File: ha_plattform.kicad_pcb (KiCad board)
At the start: 2 copper layers, 60 x 55 mm, 12 parts, among them J3 Raspberry_Pi_2_3

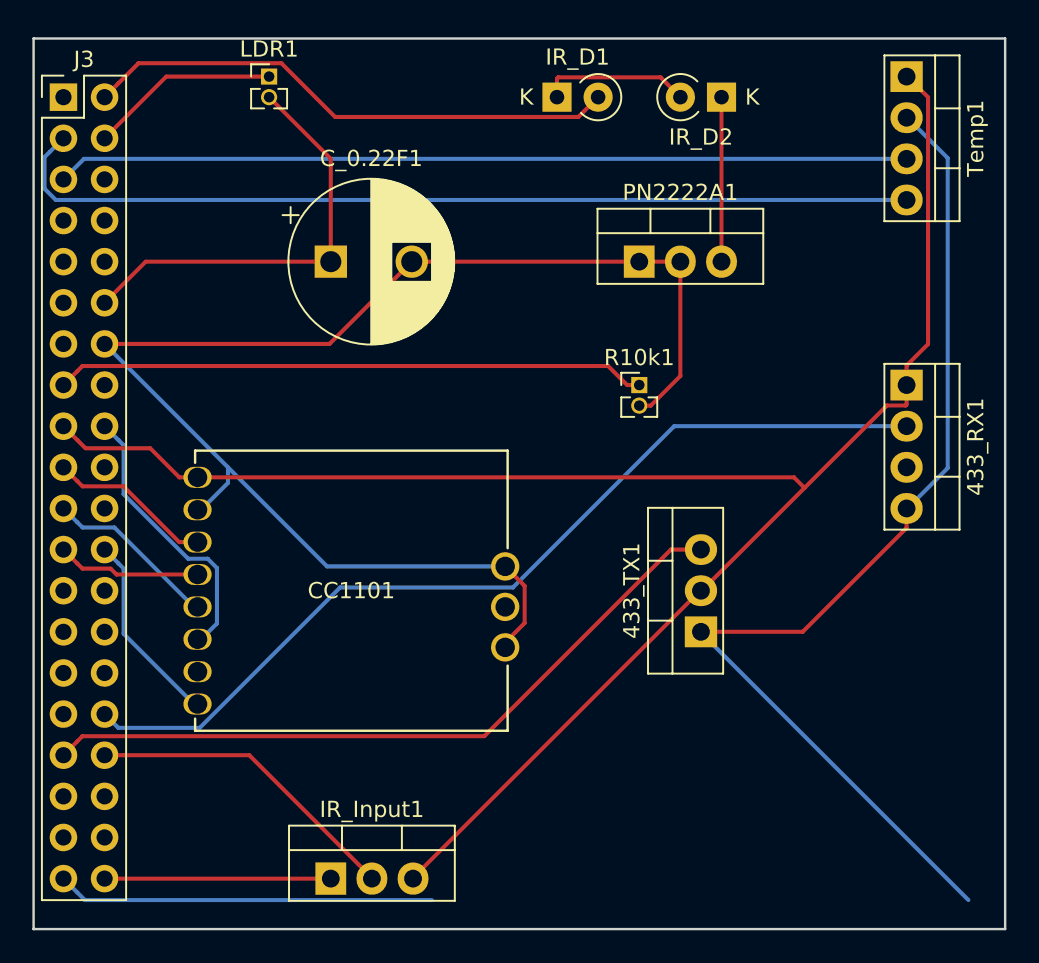
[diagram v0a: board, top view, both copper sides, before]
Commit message: Changed track width, improved routing
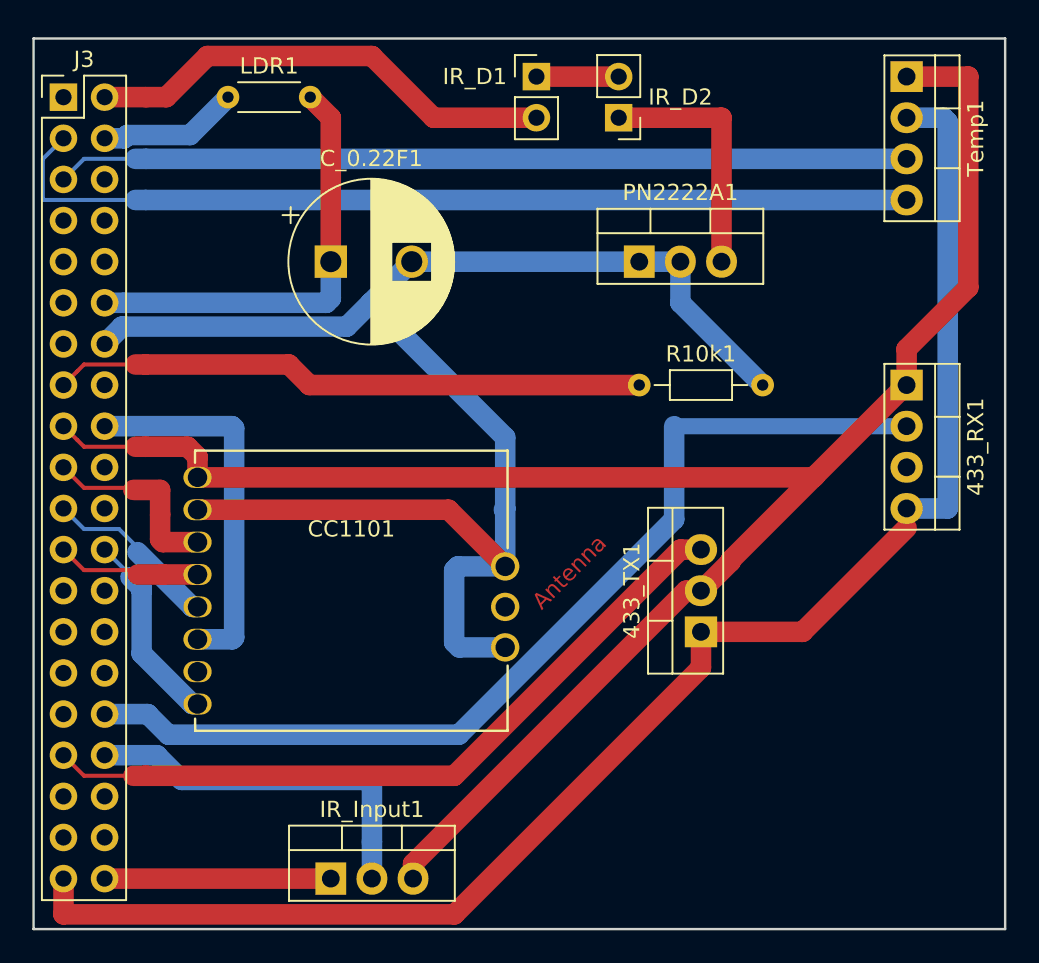
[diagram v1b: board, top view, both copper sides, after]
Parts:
- IR_D1, IR_D2: footprint Diode_THT:D_A-405_P2.54mm_Vertical_KathodeUp -> Connector_PinHeader_2.54mm:PinHeader_1x02_P2.54mm_Vertical
- LDR1: footprint Connector_PinHeader_1.27mm:PinHeader_1x02_P1.27mm_Vertical -> Resistor_THT:R_Axial_DIN0204_L3.6mm_D1.6mm_P5.08mm_Horizontal
- R10k1: footprint Connector_PinHeader_1.27mm:PinHeader_1x02_P1.27mm_Vertical -> Resistor_THT:R_Axial_DIN0204_L3.6mm_D1.6mm_P7.62mm_Horizontal
- moved IR_D2 6.48 mm to (56.1, 24.9)
- moved LDR1 2.84 mm to (32.0, 23.6)
- moved IR_D1 1.80 mm to (51.1, 22.4)
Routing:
- net Net-(CC1101-Pad11): track 88.0 -> 99.2 mm
- net Net-(433_RX1-Pad4): track 89.6 -> 95.9 mm
- net Net-(CC1101-Pad6): track 17.4 -> 23.5 mm
- net Net-(433_RX1-Pad1): track 111.4 -> 116.6 mm
- net Net-(IR_D2-Pad1): track 10.2 -> 15.2 mm
- net Net-(IR_D1-Pad1): track 9.31 -> 5.08 mm
- net Net-(IR_D1-Pad2): track 33.2 -> 29.3 mm
- net Net-(433_RX1-Pad2): track 57.6 -> 61.3 mm
- net Net-(IR_Input1-Pad2): track 19.7 -> 23.3 mm
- net Net-(J3-Pad4): track 11.7 -> 9.31 mm
- net Net-(CC1101-Pad3): track 10.2 -> 11.9 mm
- net Net-(433_TX1-Pad3): track 44.6 -> 45.7 mm
- net Net-(J3-Pad3): track 57.1 -> 57.7 mm
- net Net-(CC1101-Pad8): track 12.0 -> 12.6 mm
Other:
- net class 1.27mm added: clearance 0.127, trace_width 1.27, via_dia 0.6, via_drill 0.4
- net class Default: clearance 0.2 -> 0.127
- rule trace_clearance: 0.2 -> 0.127
- rule trace_min: 0.2 -> 0.127
- rule via_min_size: 0.4 -> 0.508
- board text added: "Antenna"

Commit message: changed details for fabrication
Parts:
- moved IR_Input1 1.14 mm to (38.4, 70.7)
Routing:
- net Net-(433_RX1-Pad4): track 95.9 -> 94.1 mm
- net Net-(IR_Input1-Pad2): track 23.3 -> 22.2 mm
- net Net-(433_RX1-Pad1): track 116.6 -> 115.7 mm
- net Net-(IR_D1-Pad2): track 29.3 -> 28.7 mm
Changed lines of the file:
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@@
     (thickness 1.6)
     (drawings 7)
-    (tracks 156)
+    (tracks 153)
     (zones 0)
     (modules 12)
@@
   )
   (module Package_TO_SOT_THT:TO-220-3_Vertical (layer F.Cu)
-    (at 38.354 71.882)
+    (at 38.354 70.739)
     (descr "TO-220-3, Vertical, RM 2.54mm, see https://www.vishay.com/docs/66542/to-220-1.pdf")
     (tags "TO-220-3 Vertical RM 2.54mm")
@@
   (segment (start 30.124 55.102) (end 29.899 55.102) (width 0.25) (layer B.Cu) (net 9) (status 30))
   (segment (start 51.054 22.352) (end 56.134 22.352) (width 1.27) (layer F.Cu) (net 12) (status 30))
-  (segment (start 51.054 24.892) (end 44.704 24.892) (width 1.27) (layer F.Cu) (net 13) (status 10))
-  (segment (start 44.704 24.892) (end 40.894 21.082) (width 1.27) (layer F.Cu) (net 13))
-  (segment (start 40.894 21.082) (end 30.734 21.082) (width 1.27) (layer F.Cu) (net 13))
-  (segment (start 30.734 21.082) (end 28.194 23.622) (width 1.27) (layer F.Cu) (net 13))
-  (segment (start 28.194 23.622) (end 26.924 23.622) (width 1.27) (layer F.Cu) (net 13))
   (segment (start 56.134 24.892) (end 62.484 24.892) (width 1.27) (layer F.Cu) (net 14) (status 10))
   (segment (start 62.484 33.782) (end 62.484 24.892) (width 1.27) (layer F.Cu) (net 14) (status 10))
   (segment (start 40.894 71.882) (end 40.894 71.9295) (width 0.25) (layer F.Cu) (net 15) (status 30))
   (segment (start 40.894 71.882) (end 40.894 71.8345) (width 0.25) (layer F.Cu) (net 15) (status 30))
-  (segment (start 38.354 71.882) (end 24.384 71.882) (width 1.27) (layer F.Cu) (net 16) (status 30))
   (segment (start 73.914 22.352) (end 73.9615 22.352) (width 0.25) (layer F.Cu) (net 17) (status 30))
   (segment (start 73.914 41.402) (end 73.9615 41.402) (width 0.25) (layer F.Cu) (net 17) (status 30))
@@
   (segment (start 76.454 25.162) (end 76.184 24.892) (width 1.27) (layer B.Cu) (net 19))
   (segment (start 76.454 49.022) (end 76.454 25.162) (width 1.27) (layer B.Cu) (net 19))
-  (segment (start 21.844 71.882) (end 21.844 74.08999) (width 1.27) (layer F.Cu) (net 19) (status 10))
-  (segment (start 61.214 58.8645) (end 61.214 56.642) (width 1.27) (layer F.Cu) (net 19) (status 20))
-  (segment (start 45.98851 74.08999) (end 61.214 58.8645) (width 1.27) (layer F.Cu) (net 19))
-  (segment (start 21.844 74.08999) (end 45.98851 74.08999) (width 1.27) (layer F.Cu) (net 19))
   (segment (start 73.914 29.972) (end 26.924 29.972) (width 1.27) (layer B.Cu) (net 3) (status 10))
   (segment (start 20.574 27.432) (end 21.844 26.162) (width 0.25) (layer B.Cu) (net 3))
@@
   (segment (start 27.813 49.403) (end 27.813 47.879) (width 1.27) (layer F.Cu) (net 11))
   (segment (start 27.813 47.879) (end 26.162 47.879) (width 1.27) (layer F.Cu) (net 11))
-  (segment (start 26.924 23.622) (end 24.384 23.622) (width 1.27) (layer F.Cu) (net 13) (status 20))
-  (segment (start 40.894 71.882) (end 40.894 69.612) (width 1.27) (layer B.Cu) (net 15) (status 10))
+  (segment (start 51.054 24.892) (end 41.148 24.892) (width 1.27) (layer F.Cu) (net 13))
+  (segment (start 41.148 24.892) (end 38.1 21.844) (width 1.27) (layer F.Cu) (net 13))
+  (segment (start 26.162 21.844) (end 24.384 23.622) (width 1.27) (layer F.Cu) (net 13))
+  (segment (start 38.1 21.844) (end 26.162 21.844) (width 1.27) (layer F.Cu) (net 13))
   (segment (start 29.13933 65.786) (end 40.894 65.786) (width 1.27) (layer B.Cu) (net 15))
   (segment (start 27.61533 64.262) (end 29.13933 65.786) (width 1.27) (layer B.Cu) (net 15))
   (segment (start 24.384 64.262) (end 27.61533 64.262) (width 1.27) (layer B.Cu) (net 15))
-  (segment (start 40.894 69.612) (end 40.894 65.786) (width 1.27) (layer B.Cu) (net 15))
+  (segment (start 40.894 65.786) (end 40.894 70.739) (width 1.27) (layer B.Cu) (net 15))
+  (segment (start 37.211 71.882) (end 38.354 70.739) (width 1.27) (layer B.Cu) (net 16))
+  (segment (start 24.384 71.882) (end 37.211 71.882) (width 1.27) (layer B.Cu) (net 16))
   (segment (start 22.693999 44.791999) (end 23.114 45.212) (width 0.25) (layer F.Cu) (net 17) (status 10))
   (segment (start 26.924 45.212) (end 29.504 45.212) (width 1.27) (layer F.Cu) (net 17))
@@
   (segment (start 60.298498 54.102) (end 61.214 54.102) (width 1.27) (layer F.Cu) (net 17))
   (segment (start 43.434 70.966498) (end 60.298498 54.102) (width 1.27) (layer F.Cu) (net 17))
-  (segment (start 43.434 71.882) (end 43.434 70.966498) (width 1.27) (layer F.Cu) (net 17))
   (segment (start 23.114 45.212) (end 26.035 45.212) (width 0.25) (layer F.Cu) (net 17))
   (segment (start 26.924 45.212) (end 26.289 45.212) (width 1.27) (layer F.Cu) (net 17))
@@
   (segment (start 24.384 61.722) (end 27.051 61.722) (width 1.27) (layer B.Cu) (net 18))
   (segment (start 27.051 61.722) (end 28.321 62.992) (width 1.27) (layer B.Cu) (net 18))
+  (segment (start 61.1665 56.642) (end 61.214 56.642) (width 1.27) (layer F.Cu) (net 19))
+  (segment (start 21.844 73.787) (end 44.0215 73.787) (width 1.27) (layer F.Cu) (net 19))
+  (segment (start 44.0215 73.787) (end 61.1665 56.642) (width 1.27) (layer F.Cu) (net 19))
+  (segment (start 21.844 71.882) (end 21.844 73.787) (width 1.27) (layer F.Cu) (net 19))
   (segment (start 61.214 51.562) (end 59.944 51.562) (width 1.27) (layer F.Cu) (net 20) (status 10))
   (segment (start 59.944 51.562) (end 45.974 65.532) (width 1.27) (layer F.Cu) (net 20))

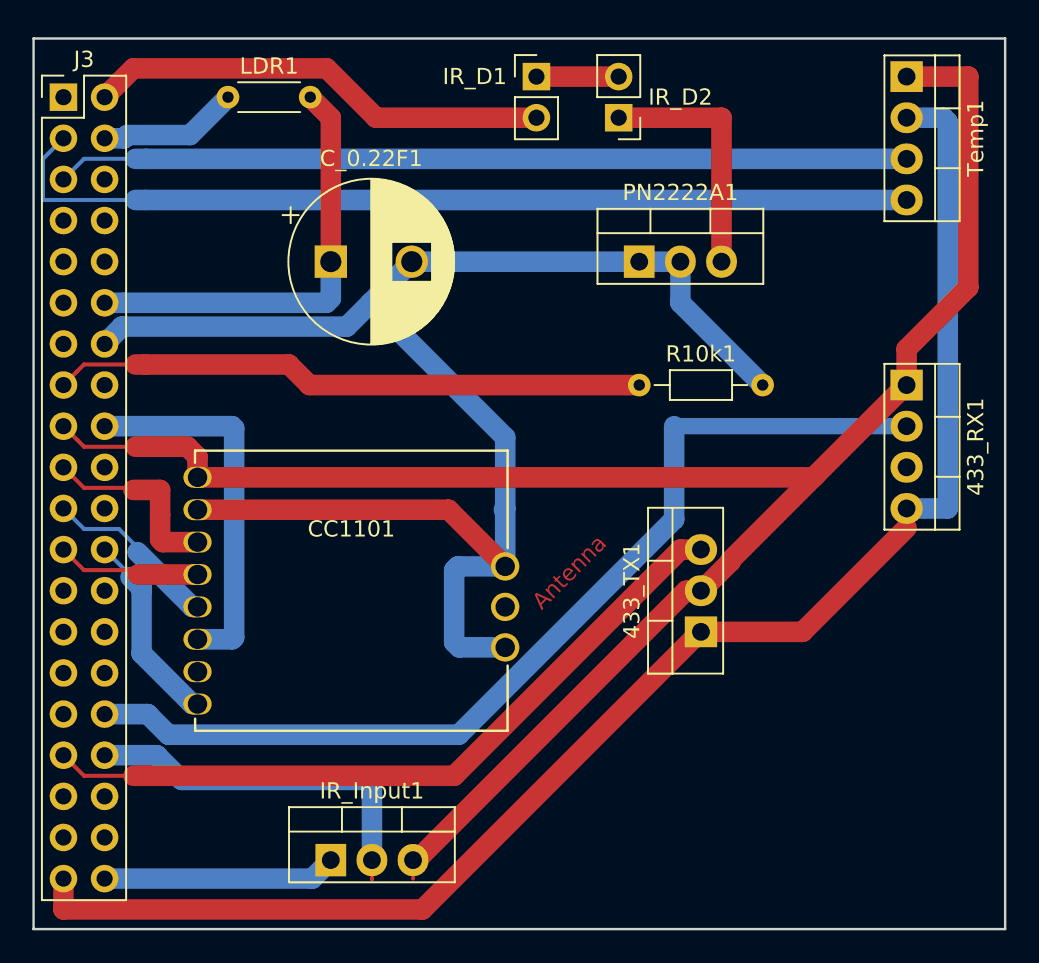
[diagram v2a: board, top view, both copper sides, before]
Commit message: Reduced layout size to fit into case
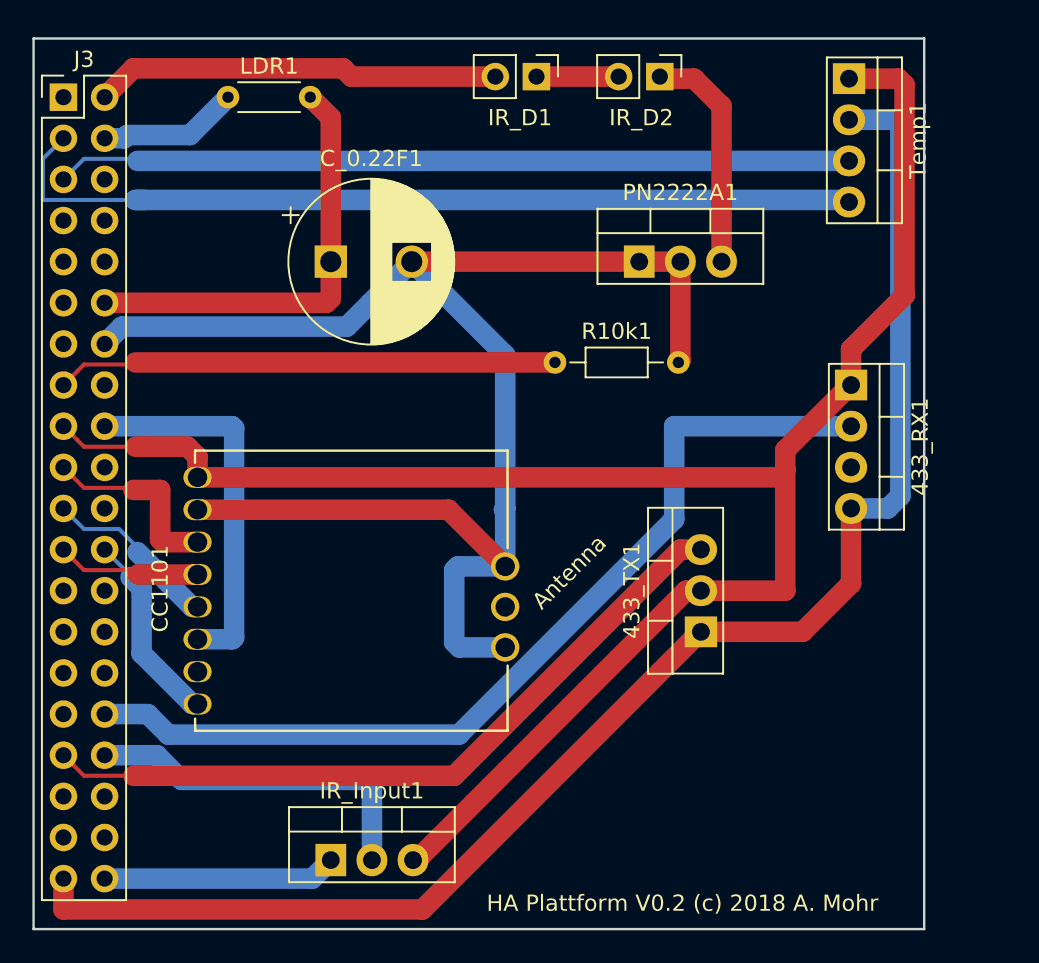
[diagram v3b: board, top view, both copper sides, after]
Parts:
- moved R10k1 5.39 mm to (52.2, 40.0)
- moved IR_D2 3.59 mm to (58.7, 22.4), turned to 270 degrees
- moved Temp1 3.56 mm to (70.4, 22.5)
- moved 433_RX1 3.43 mm to (70.5, 41.4)
- turned IR_D1 to 270 degrees
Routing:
- net Net-(J3-Pad15): track 36.2 -> 30.5 mm
- net Net-(J3-Pad5): track 52.6 -> 48.9 mm
- net Net-(IR_D1-Pad2): track 28.7 -> 25.1 mm
- net Net-(433_RX1-Pad2): track 61.3 -> 57.9 mm
- net Net-(J3-Pad3): track 57.7 -> 54.8 mm
- net Net-(CC1101-Pad11): track 99.2 -> 97.2 mm
- net Net-(433_RX1-Pad1): track 115.7 -> 114.3 mm
- net Net-(IR_D2-Pad1): track 15.2 -> 14.1 mm
- net Net-(433_RX1-Pad4): track 94.1 -> 93.1 mm
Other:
- board size 60 x 55 mm -> 55 x 55 mm
- board text added: "HA Plattform V0.2 (c) 2018 A. Mohr"
